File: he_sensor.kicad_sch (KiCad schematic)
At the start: 2 parts, among them U1 A1324LLHLT-T

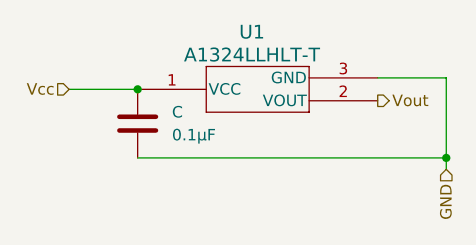
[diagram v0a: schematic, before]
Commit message: [ADD](keys) added keys subsheet
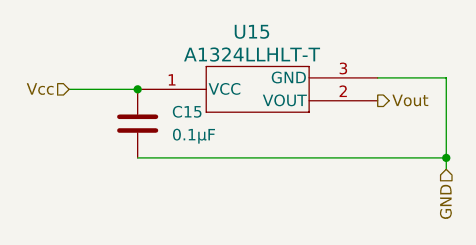
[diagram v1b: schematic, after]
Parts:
- renumbered C to C15, U1 to U15

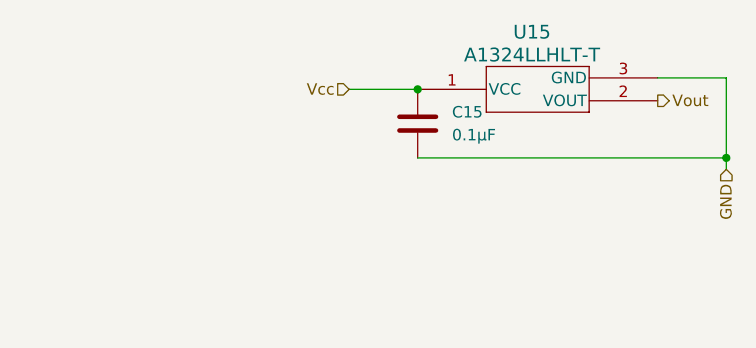
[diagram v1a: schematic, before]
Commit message: [UPDATE](TMR) switched to TMR sensors + added ldo
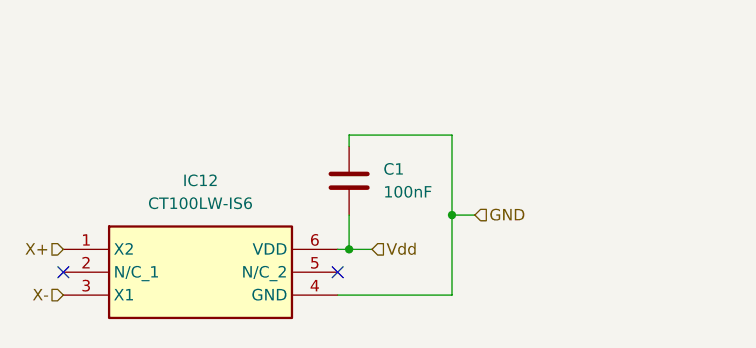
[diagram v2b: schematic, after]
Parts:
- removed C15: 0.1µF, symbol Device:C
- removed U15: A1324LLHLT-T, DIO_A1324LLHLT-T_ALM, symbol A1324:A1324LLHLT-T
- added C1: 100nF, symbol Device:C
- added IC12: CT100LW-IS6, SOT95P280X135-6N, symbol CT100LW-IS6:CT100LW-IS6
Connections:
- net GND: now also C1.2, IC12.4 (GND)
- new net Vdd: C1.1, IC12.6 (VDD)
- new net X+: IC12.1 (X2)
- new net X-: IC12.3 (X1)
- no-connect marks 0 -> 2

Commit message: [ADD](HID SPI Bridge)
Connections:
- net GND: now also C1.1; no longer C1.2
- net Vdd: now also C1.2; no longer C1.1
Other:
- moved on the sheet: C1

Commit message: [ADD](General) v1
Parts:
- renumbered C1 to C16, IC12 to IC3
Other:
- company: (none) -> Ryzzen
- title: (none) -> TMR based triple USB Keyboard

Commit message: [ADD](General) v2 split
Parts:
- renumbered C16 to C23

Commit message: [FIX](General) footprints
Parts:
- IC3: footprint SOT95P280X135-6N -> CT100LW-IS6:SOT95P280X135-6N
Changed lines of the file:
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@@
 			)
 		)
-		(property "Footprint" "SOT95P280X135-6N"
+		(property "Footprint" "CT100LW-IS6:SOT95P280X135-6N"
 			(at 156.21 190.17 0)
 			(effects

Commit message: [ADD](General) added all footprints expect leds
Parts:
- C23: footprint (none) -> Capacitor_SMD:C_0603_1608Metric_Pad1.08x0.95mm_HandSolder
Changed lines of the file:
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@@
 			)
 		)
-		(property "Footprint" ""
+		(property "Footprint" "Capacitor_SMD:C_0603_1608Metric_Pad1.08x0.95mm_HandSolder"
 			(at 164.1348 95.25 0)
 			(effects

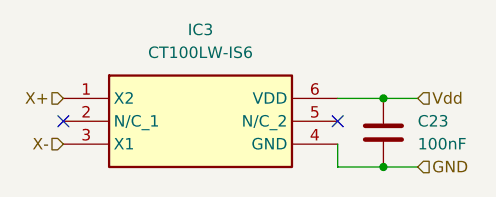
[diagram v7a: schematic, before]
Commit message: [FIX](USB) main usb net labels
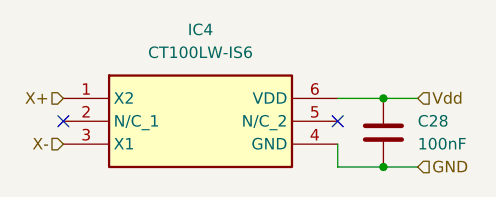
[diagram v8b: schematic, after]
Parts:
- renumbered C23 to C28, IC3 to IC4
